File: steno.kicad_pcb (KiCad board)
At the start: 4 copper layers, 200.3 x 94.7 mm, 65 parts, among them J1 USB_C_Receptacle_USB2.0_14P, SW1 SW_Push, U1 RP2040, U2 AP2127N-3.3, U3 W25Q16JVSS, Y1 12 MHz

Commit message: Smalled Caps and Restarting Layout.
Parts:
- removed C4: 100pF, Capacitor_Tantalum_SMD:CP_EIA-1608-08_AVX-J_HandSolder
- removed S1, S10, S11, S12, S13, S14, S15, S16, S17, S18, S19, S2, S20, S3, S4, S5, S6, S7, S8, S9: Keyswitch, ScottoKeebs_Hotswap:Hotswap_Choc_V1V2_1.00u
- added D22: 1N914, Diode_SMD:D_SOD-123, B.Cu at (127.0, 82.5)
- added D23: 1N914, Diode_SMD:D_SOD-123, B.Cu at (140.0, 82.5)
- added D24: 1N914, Diode_SMD:D_SOD-123, B.Cu at (193.0, 82.5)
- added D25: 1N914, Diode_SMD:D_SOD-123, B.Cu at (211.0, 82.5)
- added R6: 1k Ohms, Resistor_SMD:R_0402_1005Metric_Pad0.72x0.64mm_HandSolder, B.Cu at (161.2, 54.5)
- added REF**: MountingHole_2.2mm_M2_DIN965_Pad, MountingHole:MountingHole_2.2mm_M2_DIN965_Pad, F.Cu at (53.0, 77.0)
- added REF**: MountingHole_2.2mm_M2_DIN965_Pad, MountingHole:MountingHole_2.2mm_M2_DIN965_Pad, F.Cu at (267.0, 77.0)
- added REF**: MountingHole_2.2mm_M2_DIN965_Pad, MountingHole:MountingHole_2.2mm_M2_DIN965_Pad, F.Cu at (267.0, 39.0)
- added REF**: MountingHole_2.2mm_M2_DIN965_Pad, MountingHole:MountingHole_2.2mm_M2_DIN965_Pad, F.Cu at (53.0, 39.0)
- added S10_*1: Keyswitch, ScottoKeebs_Hotswap:Hotswap_Choc_V1V2_1.00u, F.Cu at (136.0, 65.5)
- added S11_F1: Keyswitch, ScottoKeebs_Hotswap:Hotswap_Choc_V1V2_1.00u, F.Cu at (184.0, 48.5)
- added S12_P1: Keyswitch, ScottoKeebs_Hotswap:Hotswap_Choc_V1V2_1.00u, F.Cu at (202.0, 48.5)
- added S13_L1: Keyswitch, ScottoKeebs_Hotswap:Hotswap_Choc_V1V2_1.00u, F.Cu at (220.0, 48.5)
- added S14_T1: Keyswitch, ScottoKeebs_Hotswap:Hotswap_Choc_V1V2_1.00u, F.Cu at (238.0, 48.5)
- added S15_D1: Keyswitch, ScottoKeebs_Hotswap:Hotswap_Choc_V1V2_1.00u, F.Cu at (256.0, 48.5)
- added S16_R1: Keyswitch, ScottoKeebs_Hotswap:Hotswap_Choc_V1V2_1.00u, F.Cu at (184.0, 65.5)
- added S17_B1: Keyswitch, ScottoKeebs_Hotswap:Hotswap_Choc_V1V2_1.00u, F.Cu at (202.0, 65.5)
- added S18_G1: Keyswitch, ScottoKeebs_Hotswap:Hotswap_Choc_V1V2_1.00u, F.Cu at (220.0, 65.5)
- added S19_S1: Keyswitch, ScottoKeebs_Hotswap:Hotswap_Choc_V1V2_1.00u, F.Cu at (238.0, 65.5)
- added S1_S1: Keyswitch, ScottoKeebs_Hotswap:Hotswap_Choc_V1V2_1.00u, F.Cu at (64.0, 48.5)
- added S20_Z1: Keyswitch, ScottoKeebs_Hotswap:Hotswap_Choc_V1V2_1.00u, F.Cu at (256.0, 65.5)
- added S21_O1: Keyswitch, ScottoKeebs_Hotswap:Hotswap_Choc_V1V2_1.00u, F.Cu at (136.0, 82.5)
- added S22_A1: Keyswitch, ScottoKeebs_Hotswap:Hotswap_Choc_V1V2_1.00u, F.Cu at (118.0, 82.5)
- added S23_E1: Keyswitch, ScottoKeebs_Hotswap:Hotswap_Choc_V1V2_1.00u, F.Cu at (184.0, 82.5)
- added S24_U1: Keyswitch, ScottoKeebs_Hotswap:Hotswap_Choc_V1V2_1.00u, F.Cu at (202.0, 82.5)
- added S2_T1: Keyswitch, ScottoKeebs_Hotswap:Hotswap_Choc_V1V2_1.00u, F.Cu at (82.0, 48.5)
- added S3_P1: Keyswitch, ScottoKeebs_Hotswap:Hotswap_Choc_V1V2_1.00u, F.Cu at (100.0, 48.5)
- added S4_H1: Keyswitch, ScottoKeebs_Hotswap:Hotswap_Choc_V1V2_1.00u, F.Cu at (118.0, 48.5)
- added S5_*1: Keyswitch, ScottoKeebs_Hotswap:Hotswap_Choc_V1V2_1.00u, F.Cu at (136.0, 48.5)
- added S6_S1: Keyswitch, ScottoKeebs_Hotswap:Hotswap_Choc_V1V2_1.00u, F.Cu at (64.0, 65.5)
- added S7_K1: Keyswitch, ScottoKeebs_Hotswap:Hotswap_Choc_V1V2_1.00u, F.Cu at (82.0, 65.5)
- added S8_W1: Keyswitch, ScottoKeebs_Hotswap:Hotswap_Choc_V1V2_1.00u, F.Cu at (100.0, 65.5)
- added S9_R1: Keyswitch, ScottoKeebs_Hotswap:Hotswap_Choc_V1V2_1.00u, F.Cu at (118.0, 65.5)
- added SW2: SW_Push, ScottoKeebs_Components:Button_MJTP1243, B.Cu at (156.2, 85.8)
- C1, C10, C11, C12, C13, C2, C3, C5, C6, C9: footprint Capacitor_Tantalum_SMD:CP_EIA-1608-08_AVX-J_HandSolder -> Capacitor_SMD:C_0402_1005Metric_Pad0.74x0.62mm_HandSolder; moved to B.Cu
- C7, C8, D1, U1, U2, U3: moved to B.Cu
- R1, R2, R3, R4: footprint Resistor_SMD:R_01005_0402Metric_Pad0.57x0.30mm_HandSolder -> Resistor_SMD:R_0402_1005Metric_Pad0.72x0.64mm_HandSolder
- R5: footprint Resistor_SMD:R_01005_0402Metric_Pad0.57x0.30mm_HandSolder -> Resistor_SMD:R_0402_1005Metric_Pad0.72x0.64mm_HandSolder; moved to B.Cu
- SW1: footprint Button_Switch_THT:SW_PUSH_6mm -> ScottoKeebs_Components:Button_MJTP1243; moved to B.Cu
- Y1: footprint Crystal:Crystal_SMD_3225-4Pin_3.2x2.5mm_HandSoldering -> Crystal:Crystal_SMD_3215-2Pin_3.2x1.5mm; moved to B.Cu
- moved D21 114.5 mm to (265.0, 65.5), turned to 90 degrees
- moved D16 93.4 mm to (265.0, 48.5)
- moved D6 68.2 mm to (140.0, 48.5), turned to 90 degrees
- moved D11 42.3 mm to (140.0, 65.5)
- moved D7 34.7 mm to (73.0, 65.5)
- moved D20 34.6 mm to (247.0, 65.5)
- moved D15 34.6 mm to (247.0, 48.5)
- moved D2 34.6 mm to (73.0, 48.5)
- moved C7 30.0 mm to (163.0, 52.2), turned to -90 degrees
- moved C1 29.4 mm to (154.6, 63.9)
- moved R5 29.4 mm to (154.0, 72.7), turned to 90 degrees
- moved C5 29.2 mm to (164.2, 48.4), turned to -90 degrees
- moved U3 28.9 mm to (160.0, 70.1)
- moved U1 28.5 mm to (160.0, 59.5), turned to 180 degrees
- moved C2 28.2 mm to (161.0, 65.0)
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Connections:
- D12 pad 1: ROW_1 -> ROW_3
- D13 pad 1: ROW_1 -> ROW_3
- D14 pad 1: ROW_1 -> ROW_3
- D15 pad 1: ROW_1 -> ROW_3
- D16 pad 1: ROW_1 -> ROW_3
- D17 pad 1: ROW_2 -> ROW_4
- D18 pad 1: ROW_2 -> ROW_4
- D19 pad 1: ROW_2 -> ROW_4
- D20 pad 1: ROW_2 -> ROW_4
- D21 pad 1: ROW_2 -> ROW_4
- J1 pad SH: Net-(J1-SHIELD) -> GND
- U1 pad 11: COL_8 -> ROW_4
- U1 pad 12: COL_9 -> ROW_5
- U1 pad 13: COL_10 -> unconnected-(U1-GPIO10-Pad13)
- U1 pad 14: ROW_1 -> unconnected-(U1-GPIO11-Pad14)
- U1 pad 15: ROW_2 -> unconnected-(U1-GPIO12-Pad15)
- U1 pad 2: unconnected-(U1-GPIO0-Pad2) -> COL_1
- U1 pad 26: unconnected-(U1-RUN-Pad26) -> Net-(U1-RUN)
- U1 pad 29: COL_3 -> unconnected-(U1-GPIO18-Pad29)
- U1 pad 3: unconnected-(U1-GPIO1-Pad3) -> COL_2
- U1 pad 36: COL_2 -> unconnected-(U1-GPIO24-Pad36)
- U1 pad 37: COL_1 -> unconnected-(U1-GPIO25-Pad37)
- U1 pad 4: unconnected-(U1-GPIO2-Pad4) -> COL_3
- U1 pad 5: unconnected-(U1-GPIO3-Pad5) -> COL_4
- U1 pad 6: COL_4 -> COL_5
- U1 pad 7: COL_5 -> ROW_1
- U1 pad 8: COL_6 -> ROW_2
- U1 pad 9: COL_7 -> ROW_3
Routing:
- net ROW_1: track 458.5 -> 0.00 mm, vias 5 -> 0
- net ROW_2: track 404.5 -> 0.00 mm, vias 5 -> 0
- net COL_2: track 118.5 -> 0.00 mm, vias 5 -> 0
- net COL_3: track 114.2 -> 0.00 mm, vias 3 -> 0
- net COL_9: track 111.9 -> 0.00 mm, vias 3 -> 0
- net COL_8: track 101.5 -> 0.00 mm, vias 7 -> 0
- net COL_1: track 115.0 -> 17.0 mm, vias 3 -> 0
- net COL_7: track 91.7 -> 0.00 mm, vias 3 -> 0
- net COL_4: track 81.5 -> 0.00 mm, vias 3 -> 0
- net COL_5: track 79.1 -> 0.00 mm, vias 3 -> 0
- net COL_6: track 68.9 -> 0.00 mm, vias 1 -> 0
- net COL_10: track 57.4 -> 0.00 mm, vias 3 -> 0
- net GND: track 54.4 -> 0.00 mm, vias 24 -> 0
- net +3.3V: track 54.1 -> 3.80 mm, vias 13 -> 0
- net D+: track 36.7 -> 0.00 mm, vias 2 -> 0
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- removed copper zone on B.Cu, net (none)
- removed copper zone on F.Cu, net (none)
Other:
- board size 200.3 x 94.7 mm -> 220 x 59 mm

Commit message: Layout changes & wiring testing
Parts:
- added C1: 110nF, Capacitor_SMD:C_0402_1005Metric_Pad0.74x0.62mm_HandSolder, B.Cu at (155.6, 101.5)
- added C1: 110nF, Capacitor_SMD:C_0402_1005Metric_Pad0.74x0.62mm_HandSolder, B.Cu at (149.6, 105.8)
- added C1: 110nF, Capacitor_SMD:C_0402_1005Metric_Pad0.74x0.62mm_HandSolder, B.Cu at (144.7, 97.5)
- added C1: 110nF, Capacitor_SMD:C_0402_1005Metric_Pad0.74x0.62mm_HandSolder, B.Cu at (145.3, 102.1)
- added C2: 110nF, Capacitor_SMD:C_0402_1005Metric_Pad0.74x0.62mm_HandSolder, F.Cu at (150.0, 89.4)
- C2: moved to F.Cu
- moved D16 91.5 mm to (183.1, 89.4)
- moved D21 91.5 mm to (183.1, 106.4)
- moved S15_D1 91.5 mm to (174.1, 89.4)
- moved S20_Z1 91.5 mm to (174.1, 106.4)
- moved D12 74.4 mm to (255.1, 89.4)
- moved D17 74.4 mm to (255.1, 106.4)
- moved S11_F1 74.4 mm to (246.1, 89.4)
- moved S16_R1 74.4 mm to (246.1, 106.4)
- moved D15 61.5 mm to (201.1, 89.4)
- moved D20 61.5 mm to (201.1, 106.4)
- moved S14_T1 61.5 mm to (192.1, 89.4)
- moved S19_S1 61.5 mm to (192.1, 106.4)
- moved C7 59.3 mm to (147.1, 109.4)
- moved Y1 58.0 mm to (150.1, 109.4), turned to 180 degrees
- moved C8 57.3 mm to (153.1, 109.4)
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- renumbered SW1 to BOOTSEL1, SW2 to RST1
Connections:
- S23_E1 pad 1: COL_1 -> COL_3
- U1 pad 11: ROW_4 -> unconnected-(U1-GPIO8-Pad11)
- U1 pad 12: ROW_5 -> unconnected-(U1-GPIO9-Pad12)
- U1 pad 2: COL_1 -> ROW_3
- U1 pad 3: COL_2 -> ROW_4
- U1 pad 37: unconnected-(U1-GPIO25-Pad37) -> ROW_5
- U1 pad 4: COL_3 -> COL_5
- U1 pad 40: unconnected-(U1-GPIO28/ADC2-Pad40) -> ROW_2
- U1 pad 41: unconnected-(U1-GPIO29/ADC3-Pad41) -> ROW_1
- U1 pad 6: COL_5 -> COL_3
- U1 pad 7: ROW_1 -> COL_2
- U1 pad 8: ROW_2 -> COL_1
- U1 pad 9: ROW_3 -> unconnected-(U1-GPIO7-Pad9)
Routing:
- net COL_1: track 17.0 -> 350.1 mm
- net COL_2: track 0.00 -> 298.7 mm
- net COL_3: track 0.00 -> 241.4 mm
- net COL_4: track 0.00 -> 176.1 mm
- net ROW_5: track 0.00 -> 131.5 mm
- net COL_5: track 0.00 -> 121.4 mm
- net ROW_4: track 0.00 -> 114.7 mm, vias 0 -> 8
- net ROW_3: track 0.00 -> 109.0 mm, vias 0 -> 10
- net ROW_1: track 0.00 -> 99.2 mm, vias 0 -> 8
- net ROW_2: track 0.00 -> 92.4 mm, vias 0 -> 8
- net GND: track 0.00 -> 67.4 mm, vias 0 -> 41
- net +3.3V: track 3.80 -> 68.4 mm, vias 0 -> 14
- net QSPI_SD3: track 0.00 -> 19.2 mm
- net QSPI_SCLK: track 0.00 -> 18.0 mm
- net Net-(D1-A): track 0.00 -> 17.7 mm, vias 0 -> 1
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- added copper zone on B.Cu, net (none)
- added copper zone on F.Cu, net (none)

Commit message: Updated images!
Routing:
- net GND: vias 41 -> 42
- net +3.3V: vias 14 -> 15
- net (no net): vias 5 -> 3

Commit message: Organizing docs
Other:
- outline, holes or cut-outs redrawn
- board text added: "101mm"
- board text added: "14.9mm"
- board text added: "15mm"
- board text added: "20mm"
- board text added: "220mm"
- board text added: "3mm"
- board text added: "44mm"
- board text added: "59mm"
- board text added: "9.1mm"

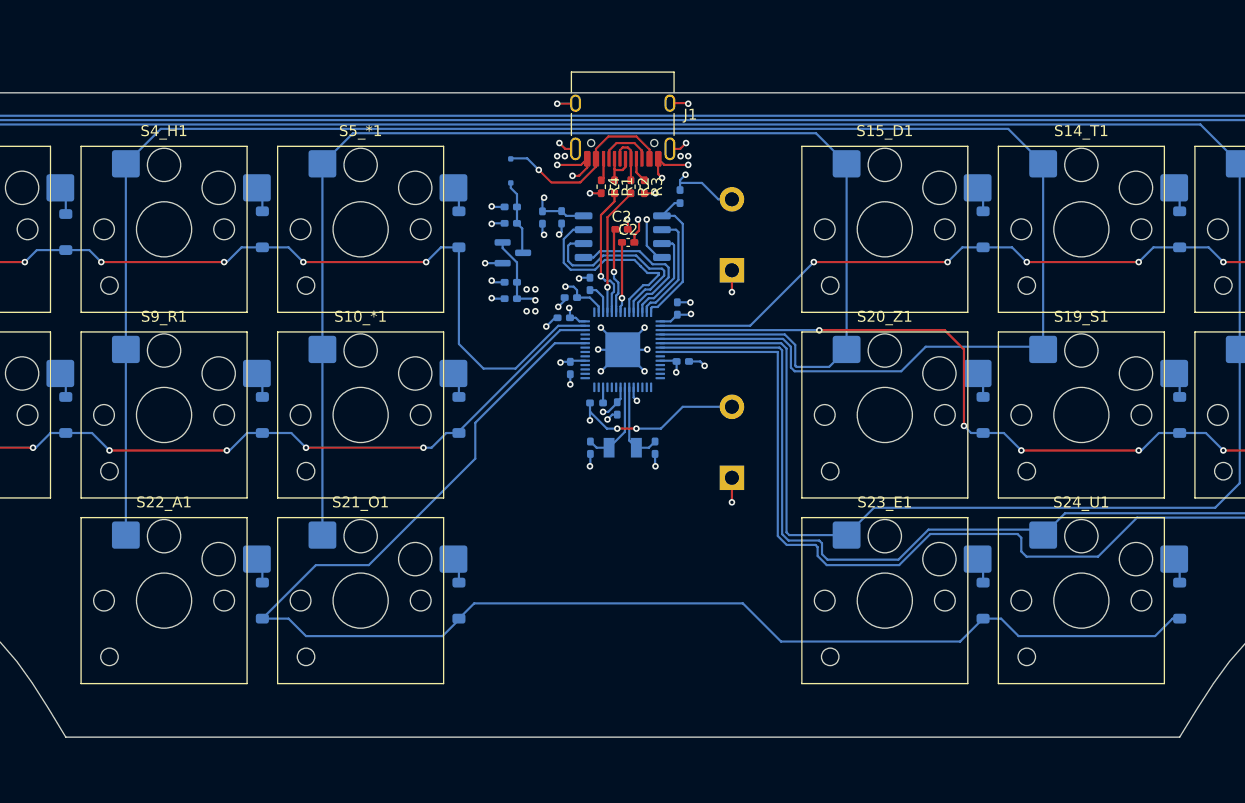
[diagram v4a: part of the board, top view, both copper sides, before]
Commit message: Fixing buttons / Transitioning to new computer.
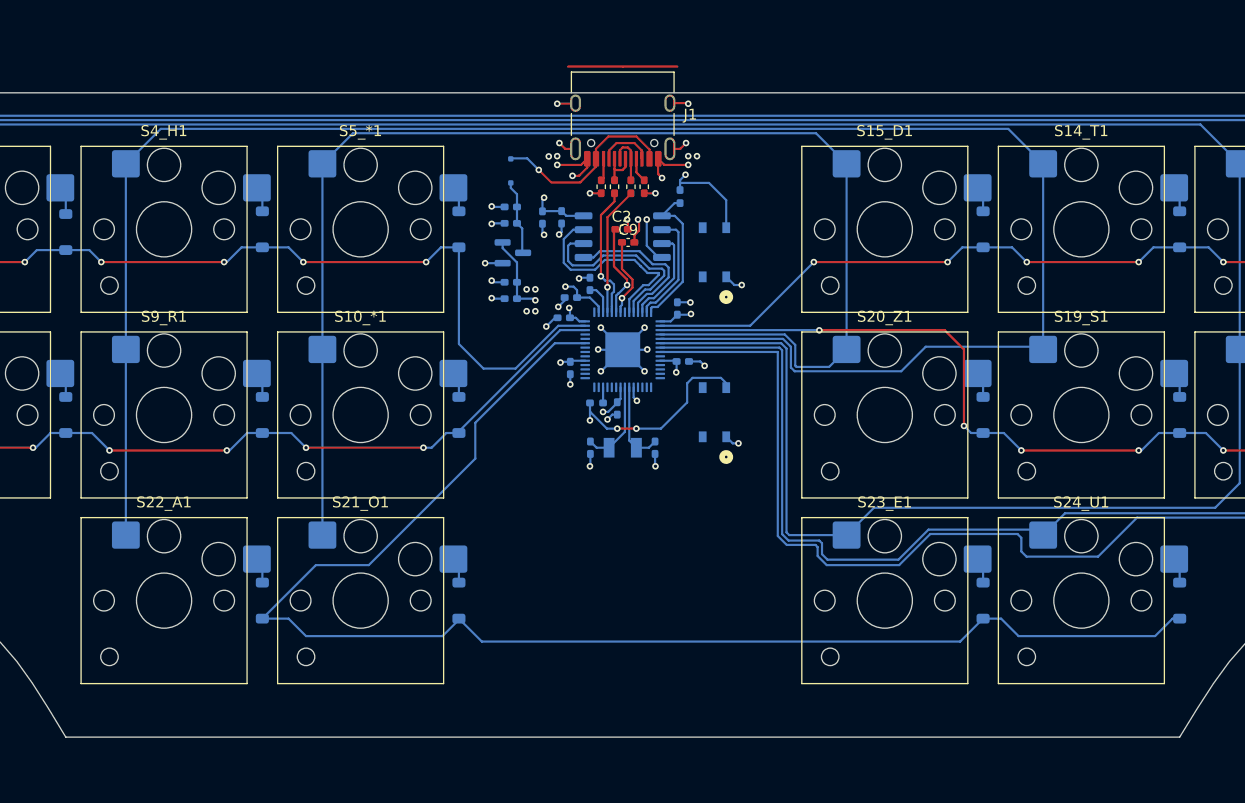
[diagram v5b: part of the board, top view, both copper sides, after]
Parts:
- BOOTSEL1, RST1: footprint ScottoKeebs_Components:Button_MJTP1243 -> 3rd_party_footprints:SW4_PTS815 SJM 250 SMTR LFS_CNK
- moved RST1 6.21 mm to (158.5, 106.1)
- moved BOOTSEL1 2.30 mm to (158.5, 91.5)
- renumbered C12 to C1, C1 to C10, C3 to C11, C6 to C12, C10 to C2, C11 to C3, C9 to C4, C13 to C5, C5 to C6, C8 to C7, C7 to C8, C2 to C9, D25 to D10, D4 to D11, D9 to D12, D14 to D13, D19 to D14, D24 to D15, D5 to D16, D10 to D17, D15 to D18, D20 to D19, D22 to D20, D6 to D21, D11 to D22, D16 to D23, D21 to D24, D23 to D25, D7 to D3, D12 to D4, D17 to D5, D3 to D6, D8 to D7, D13 to D8, D18 to D9, R5 to R1, R3 to R2, R4 to R3, R2 to R4, R1 to R5, U3 to U1, U1 to U3
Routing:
- net +3.3V: track 68.4 -> 74.2 mm, vias 15 -> 14
- net ROW_5: track 131.5 -> 130.4 mm
- net GND: track 67.4 -> 66.2 mm, vias 42 -> 44
- net (no net): vias 3 -> 2
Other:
- board text added: "102mm"
- board text removed: "101mm"
